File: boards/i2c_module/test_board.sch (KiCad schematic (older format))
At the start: 9 parts

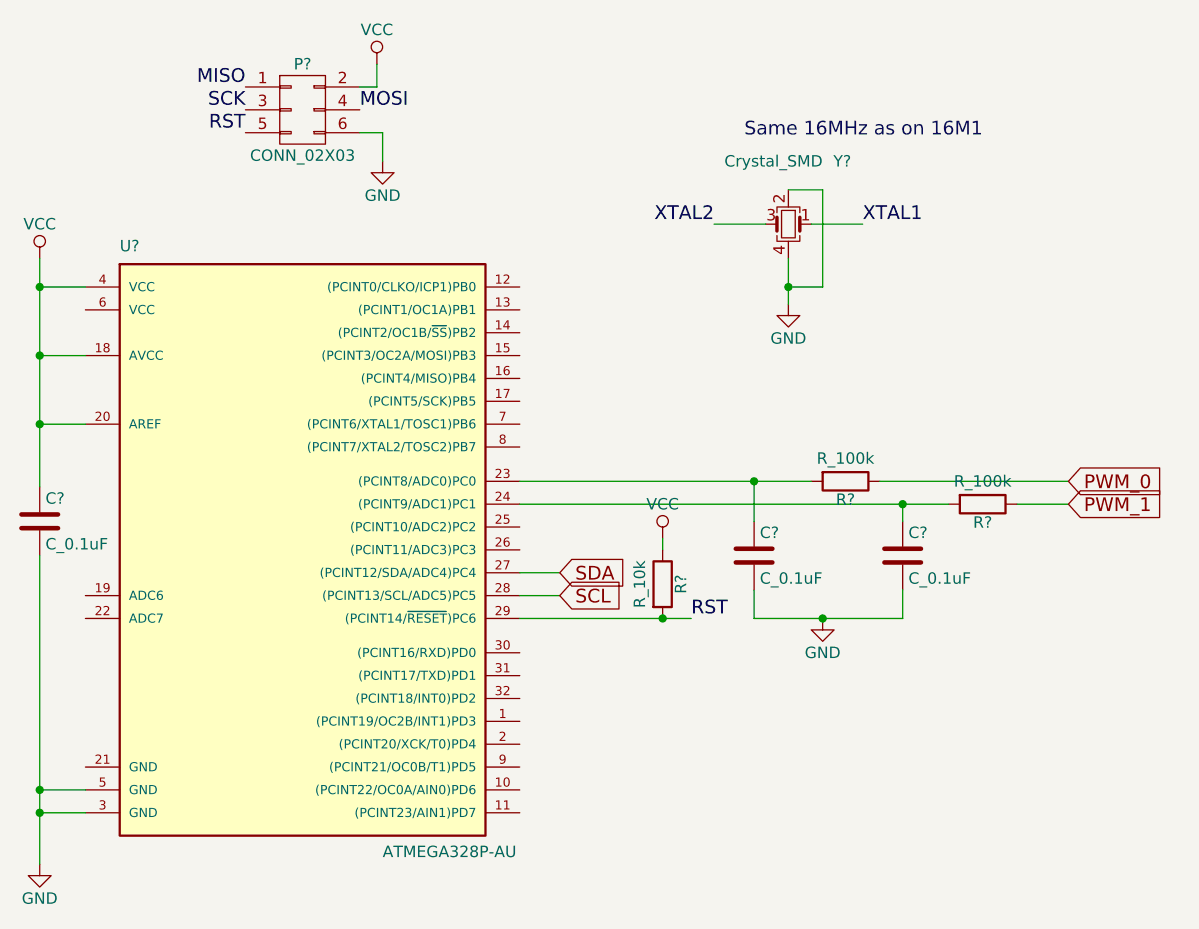
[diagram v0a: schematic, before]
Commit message: Added load caps on oscillator
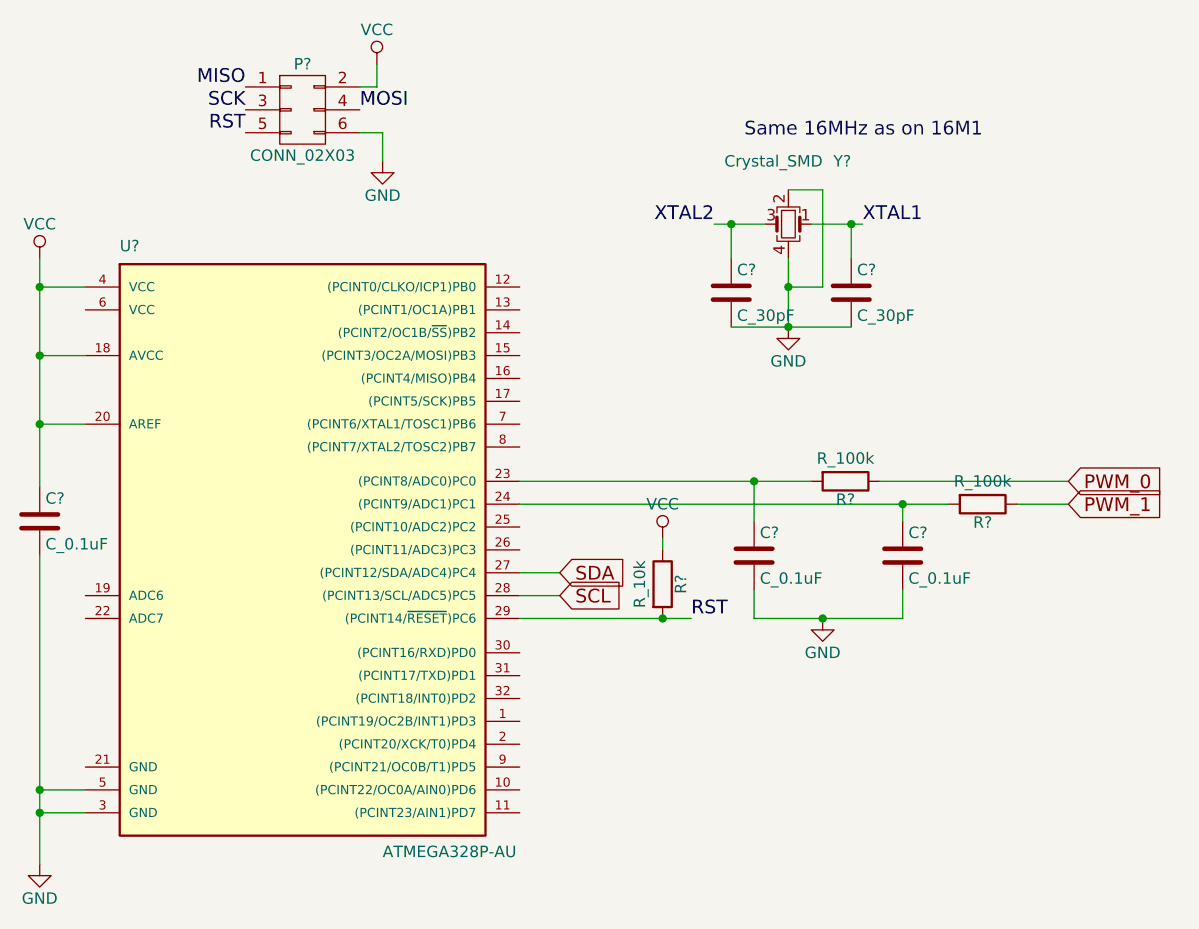
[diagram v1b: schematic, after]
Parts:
- added C? (x2): C_30pF, footprints:C_0805_OEM, symbol C_30pF
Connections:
- net GND: now also C?.2, C?.2
- net XTAL1: now also C?.1
- net XTAL2: now also C?.1
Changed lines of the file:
@@
 LIBS:valves
 LIBS:formula
+LIBS:test_board-cache
 EELAYER 25 0
 EELAYER END
@@
 $EndComp
 Wire Wire Line
-	5450 4050 6200 4050
+	5450 4050 6075 4050
+Wire Wire Line
+	6075 4050 6200 4050
 $Comp
 L VCC #PWR?
@@
 $EndComp
 Wire Wire Line
-	3350 2475 3350 3475
+	3350 2475 3350 2600
+Wire Wire Line
+	3350 2600 3350 2900
+Wire Wire Line
+	3350 2900 3350 3200
+Wire Wire Line
+	3350 3200 3350 3475
 Wire Wire Line
 	3350 2600 3550 2600
@@
 Connection ~ 3350 2900
 Wire Wire Line
-	3350 3775 3350 5125
+	3350 3775 3350 4800
+Wire Wire Line
+	3350 4800 3350 4900
+Wire Wire Line
+	3350 4900 3350 5125
 Wire Wire Line
 	3350 4800 3550 4800
@@
 $EndComp
 Wire Wire Line
-	6475 4050 7125 4050
+	6475 4050 6775 4050
+Wire Wire Line
+	6775 4050 7125 4050
 Wire Wire Line
 	7125 4050 7125 3925
@@
 Connection ~ 6775 4050
 Wire Wire Line
-	5450 3450 6725 3450
+	5450 3450 6475 3450
+Wire Wire Line
+	6475 3450 6725 3450
 Wire Wire Line
 	6475 3625 6475 3450
@@
 	7125 3625 7125 3550
 Wire Wire Line
-	5450 3550 7325 3550
+	5450 3550 7125 3550
+Wire Wire Line
+	7125 3550 7325 3550
 Connection ~ 7125 3550
 Text GLabel 7850 3450 2    60   Input ~ 0
@@
 L GND #PWR?
 U 1 1 5A74D7D2
-P 6625 2675
-F 0 "#PWR?" H 6625 2425 50  0001 C CNN
-F 1 "GND" H 6625 2525 50  0000 C CNN
-F 2 "" H 6625 2675 50  0001 C CNN
-F 3 "" H 6625 2675 50  0001 C CNN
-	1    6625 2675
-	1    0    0    -1
-$EndComp
-Wire Wire Line
-	6625 2675 6625 2475
+P 6625 2775
+F 0 "#PWR?" H 6625 2525 50  0001 C CNN
+F 1 "GND" H 6625 2625 50  0000 C CNN
+F 2 "" H 6625 2775 50  0001 C CNN
+F 3 "" H 6625 2775 50  0001 C CNN
+	1    6625 2775
+	1    0    0    -1
+$EndComp
+Wire Wire Line
+	6625 2775 6625 2600
+Wire Wire Line
+	6625 2600 6625 2475
 Wire Wire Line
 	6625 2175 6775 2175
@@
 Connection ~ 6625 2600
 Wire Wire Line
-	6725 2325 6950 2325
+	6725 2325 6900 2325
+Wire Wire Line
+	6900 2325 6950 2325
 Text Label 6950 2325 0    60   ~ 0
 XTAL1
 Wire Wire Line
-	6525 2325 6300 2325
+	6525 2325 6375 2325
+Wire Wire Line
+	6375 2325 6300 2325
 Text Label 6300 2325 2    60   ~ 0
 XTAL2
 Text Notes 7475 1950 2    60   ~ 0
 Same 16MHz as on 16M1
+$Comp
+L C_30pF C?
+U 1 1 5A74D2E7
+P 6900 2625
+F 0 "C?" H 6925 2725 50  0000 L CNN
+F 1 "C_30pF" H 6925 2525 50  0000 L CNN
+F 2 "footprints:C_0805_OEM" H 6938 2475 50  0001 C CNN
+F 3 "https://media.digikey.com/pdf/Data%20Sheets/Samsung%20PDFs/CL_Series_MLCC_ds.pdf" H 6925 2725 50  0001 C CNN
+F 4 "1276-1130-1-ND" H 6900 2625 60  0001 C CNN "MPN"
+F 5 "Digi-Key" H 6900 2625 60  0001 C CNN "MFN"
+F 6 "Value" H 6900 2625 60  0001 C CNN "Package"
+F 7 "https://www.digikey.com/product-detail/en/samsung-electro-mechanics-america-inc/CL21C300JBANNNC/1276-1130-1-ND/3889216" H 7325 3125 60  0001 C CNN "PurchasingLink"
+	1    6900 2625
+	1    0    0    -1
+$EndComp
+$Comp
+L C_30pF C?
+U 1 1 5A74D38A
+P 6375 2625
+F 0 "C?" H 6400 2725 50  0000 L CNN
+F 1 "C_30pF" H 6400 2525 50  0000 L CNN
+F 2 "footprints:C_0805_OEM" H 6413 2475 50  0001 C CNN
+F 3 "https://media.digikey.com/pdf/Data%20Sheets/Samsung%20PDFs/CL_Series_MLCC_ds.pdf" H 6400 2725 50  0001 C CNN
+F 4 "1276-1130-1-ND" H 6375 2625 60  0001 C CNN "MPN"
+F 5 "Digi-Key" H 6375 2625 60  0001 C CNN "MFN"
+F 6 "Value" H 6375 2625 60  0001 C CNN "Package"
+F 7 "https://www.digikey.com/product-detail/en/samsung-electro-mechanics-america-inc/CL21C300JBANNNC/1276-1130-1-ND/3889216" H 6800 3125 60  0001 C CNN "PurchasingLink"
+	1    6375 2625
+	1    0    0    -1
+$EndComp
+Wire Wire Line
+	6375 2475 6375 2325
+Connection ~ 6375 2325
+Wire Wire Line
+	6900 2475 6900 2325
+Connection ~ 6900 2325
+Wire Wire Line
+	6375 2775 6625 2775
+Wire Wire Line
+	6625 2775 6900 2775
+Connection ~ 6625 2775
 $EndSCHEMATC

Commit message: Changed package to TQFP from PDIP
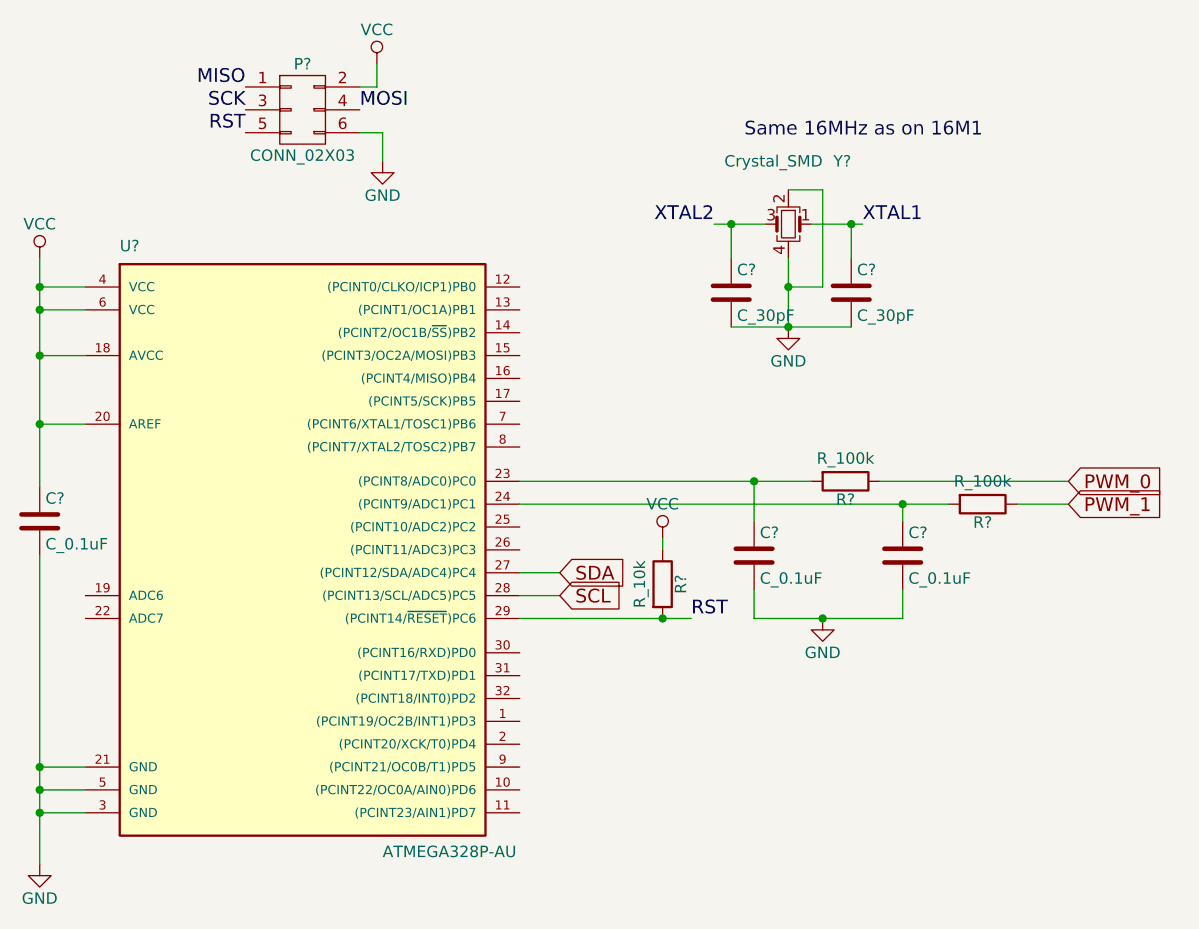
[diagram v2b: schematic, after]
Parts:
- removed U?: ATMEGA328P-AU, Housings_QFP:TQFP-32_7x7mm_Pitch0.8mm, symbol ATMEGA328P-AU
- added U?: ATMEGA328P-AU, Housings_QFP:TQFP-32_7x7mm_Pitch0.8mm, symbol ATMEGA328P-AU
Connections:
- net GND: now also U?.21 (GND), U?.3 (GND), U?.5 (GND)
- net RST: now also U?.29 ((PCINT14/~RESET~)PC6)
- net SCL: now also U?.28 ((PCINT13/SCL/ADC5)PC5)
- net SDA: now also U?.27 ((PCINT12/SDA/ADC4)PC4)
- net VCC: now also U?.18 (AVCC), U?.20 (AREF), U?.4 (VCC), U?.6 (VCC)
- net at C?.1, R?.2: now also U?.23 ((PCINT8/ADC0)PC0)
- net at C?.1, R?.2: now also U?.24 ((PCINT9/ADC1)PC1)
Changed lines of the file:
@@
 $EndComp
 Wire Wire Line
-	5450 4050 6075 4050
-Wire Wire Line
-	6075 4050 6200 4050
+	5450 4050 6200 4050
 $Comp
 L VCC #PWR?
@@
 $EndComp
 Wire Wire Line
-	3350 2475 3350 2600
-Wire Wire Line
-	3350 2600 3350 2900
-Wire Wire Line
-	3350 2900 3350 3200
-Wire Wire Line
-	3350 3200 3350 3475
+	3350 2475 3350 3475
 Wire Wire Line
 	3350 2600 3550 2600
@@
 Connection ~ 3350 2900
 Wire Wire Line
-	3350 3775 3350 4800
-Wire Wire Line
-	3350 4800 3350 4900
-Wire Wire Line
-	3350 4900 3350 5125
+	3350 3775 3350 5125
 Wire Wire Line
 	3350 4800 3550 4800
@@
 $EndComp
 Connection ~ 3350 4900
-$Comp
-L ATMEGA328P-AU U?
-U 1 1 5A74CCBF
-P 4450 3700
-F 0 "U?" H 3700 4950 50  0000 L BNN
-F 1 "ATMEGA328P-AU" H 4850 2300 50  0000 L BNN
-F 2 "Housings_QFP:TQFP-32_7x7mm_Pitch0.8mm" H 4450 3700 50  0001 C CIN
-F 3 "" H 4450 3700 50  0001 C CNN
-	1    4450 3700
-	1    0    0    -1
-$EndComp
 Wire Wire Line
 	5450 3950 5625 3950
@@
 $EndComp
 Wire Wire Line
-	6475 4050 6775 4050
-Wire Wire Line
-	6775 4050 7125 4050
+	6475 4050 7125 4050
 Wire Wire Line
 	7125 4050 7125 3925
@@
 Connection ~ 6775 4050
 Wire Wire Line
-	5450 3450 6475 3450
-Wire Wire Line
-	6475 3450 6725 3450
+	5450 3450 6725 3450
 Wire Wire Line
 	6475 3625 6475 3450
@@
 	7125 3625 7125 3550
 Wire Wire Line
-	5450 3550 7125 3550
-Wire Wire Line
-	7125 3550 7325 3550
+	5450 3550 7325 3550
 Connection ~ 7125 3550
 Text GLabel 7850 3450 2    60   Input ~ 0
@@
 $EndComp
 Wire Wire Line
-	6625 2775 6625 2600
-Wire Wire Line
-	6625 2600 6625 2475
+	6625 2475 6625 2775
 Wire Wire Line
 	6625 2175 6775 2175
@@
 Connection ~ 6625 2600
 Wire Wire Line
-	6725 2325 6900 2325
-Wire Wire Line
-	6900 2325 6950 2325
+	6725 2325 6950 2325
 Text Label 6950 2325 0    60   ~ 0
 XTAL1
 Wire Wire Line
-	6525 2325 6375 2325
-Wire Wire Line
-	6375 2325 6300 2325
+	6300 2325 6525 2325
 Text Label 6300 2325 2    60   ~ 0
 XTAL2
@@
 Connection ~ 6900 2325
 Wire Wire Line
-	6375 2775 6625 2775
-Wire Wire Line
-	6625 2775 6900 2775
+	6375 2775 6900 2775
 Connection ~ 6625 2775
+$Comp
+L ATMEGA328P-AU U?
+U 1 1 5A790AA3
+P 4450 3700
+F 0 "U?" H 3700 4950 50  0000 L BNN
+F 1 "ATMEGA328P-AU" H 4850 2300 50  0000 L BNN
+F 2 "Housings_QFP:TQFP-32_7x7mm_Pitch0.8mm" H 4450 3700 50  0001 C CIN
+F 3 "" H 4450 3700 50  0001 C CNN
+	1    4450 3700
+	1    0    0    -1
+$EndComp
+Wire Wire Line
+	3550 4700 3350 4700
+Connection ~ 3350 4700
+Wire Wire Line
+	3550 2700 3350 2700
+Connection ~ 3350 2700
 $EndSCHEMATC
